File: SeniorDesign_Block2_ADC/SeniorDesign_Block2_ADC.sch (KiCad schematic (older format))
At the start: 2 parts

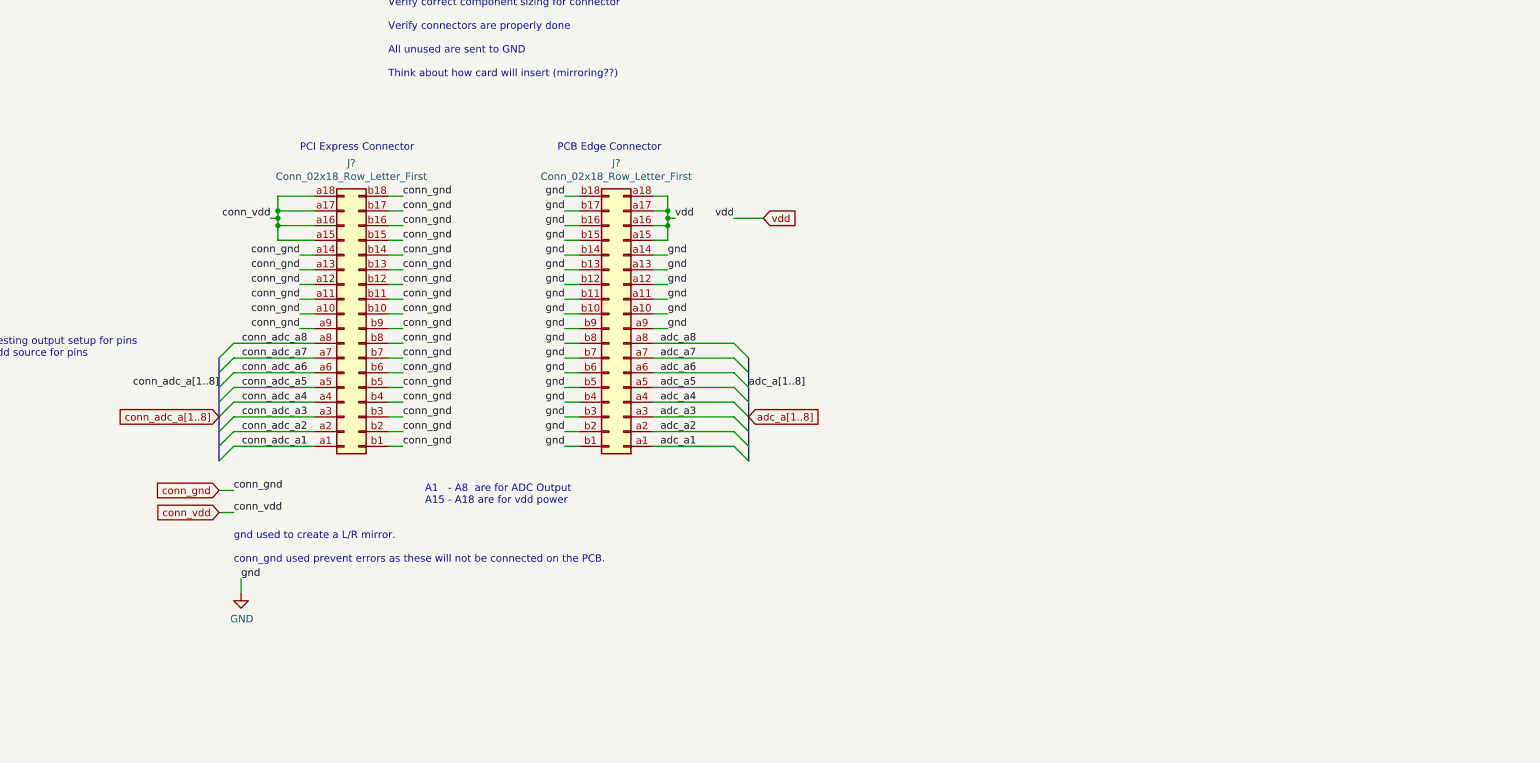
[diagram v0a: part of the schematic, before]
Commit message: Added ADC, oscillator, and misc parts associated to the two
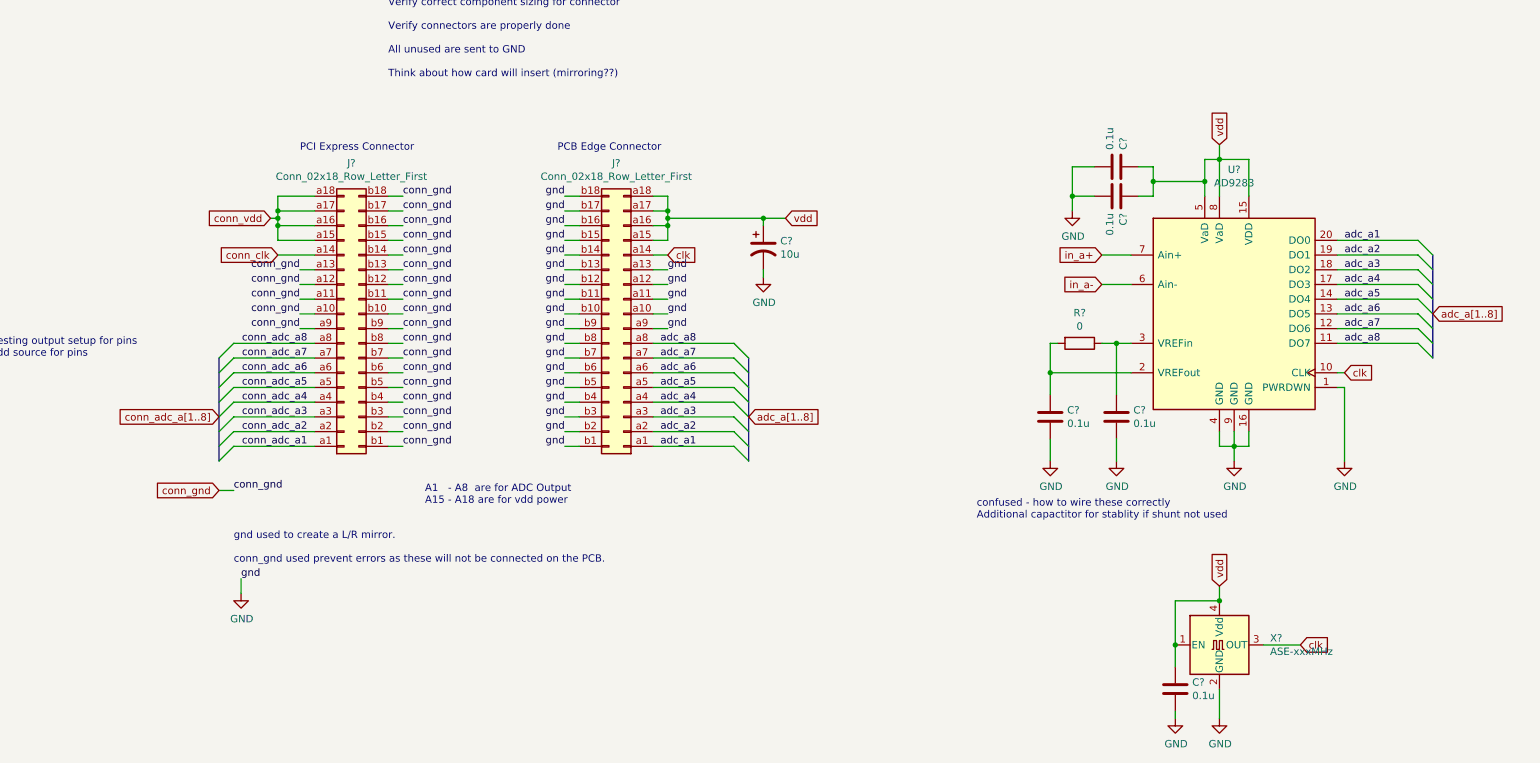
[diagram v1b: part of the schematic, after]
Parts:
- added C? (x5): 0.1u, Capacitor_SMD:C_0603_1608Metric, symbol Device:C
- added C?: 10u, Capacitor_SMD:CP_Elec_4x3.9, symbol Device:CP1
- added R?: 0, Resistor_SMD:R_0612_1632Metric_Pad1.18x3.40mm_HandSolder, symbol Device:R
- added U?: AD9283, symbol Analog_ADC:AD9283
- added X?: ASE-xxxMHz, SeniorDesign_Block2_ADC:DSC6001JI1A_Oscillator, symbol Oscillator:ASE-xxxMHz
- J?: part_url (none) -> NA
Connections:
- net GND: now also C?.2, C?.2, C?.2, C?.2, C?.2, C?.2, U?.1 (PWRDWN), U?.16 (GND), U?.4 (GND), U?.9 (GND), X?.2 (GND); no longer J?.a14 (Pin_a14)
- net adc_a1: now also U?.20 (DO0)
- net adc_a2: now also U?.19 (DO1)
- net adc_a3: now also U?.18 (DO2)
- net adc_a4: now also U?.17 (DO3)
- net adc_a5: now also U?.14 (DO4)
- net adc_a6: now also U?.13 (DO5)
- net adc_a7: now also U?.12 (DO6)
- net adc_a8: now also U?.11 (DO7)
- net conn_gnd: no longer J?.a14 (Pin_a14)
- net vdd: now also C?.1, C?.1, C?.1, C?.1, U?.15 (VDD), U?.5 (VaD), U?.8 (VaD), X?.1 (EN), X?.4 (Vdd)
- new net: C?.1, R?.2, U?.2 (VREFout)
- new net: C?.1, R?.1, U?.3 (VREFin)
- new net clk: J?.a14 (Pin_a14), U?.10 (CLK), X?.3 (OUT)
- new net conn_clk: J?.a14 (Pin_a14)
- new net in_a+: U?.7 (Ain+)
- new net in_a-: U?.6 (Ain-)
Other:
- note added: "confused - how to wire these correctly\nAdditional capactitor for stablity if shunt not used\n"

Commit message: Base shcematic complete.  Converting to PCB with misc connection errors.
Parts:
- added C3, C4: 56pF +/-5%, Capacitor_SMD:C_0603_1608Metric, symbol Device:C
- added D1: LED, LED_SMD:LED_1206_3216Metric, symbol Device:LED
- added R1, R2: 49.9 +/-1%, Resistor_SMD:R_0603_1608Metric_Pad0.98x0.95mm_HandSolder, symbol Device:R
- added R4: 0, Resistor_SMD:R_0612_1632Metric_Pad1.18x3.40mm_HandSolder, symbol Device:R
- added R5: 470, Resistor_SMD:R_0603_1608Metric_Pad0.98x0.95mm_HandSolder, symbol Device:R
- C1, C2, C5, C6, C8: renamed from C?; part_url (none) -> https://www.digikey.com/en/products/detail/samsung-electro-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
- R3: renamed from R?; part_url (none) -> NA
- U1: renamed from U?; footprint (none) -> Package_SO:SSOP-20_5.3x7.2mm_P0.65mm
- gave numbers to parts that had none: 4
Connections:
- net GND: now also C3.2, C4.2, D1.1 (K), R4.2; no longer U1.1 (PWRDWN)
- net in_a+: now also R1.2; no longer U1.7 (Ain+)
- net in_a-: now also R2.2; no longer U1.6 (Ain-)
- net vdd: now also R5.1
- new net: R4.1, U1.1 (PWRDWN)
- new net: C4.1, R2.1, U1.6 (Ain-)
- new net: C3.1, R1.1, U1.7 (Ain+)
- new net: D1.2 (A), R5.2
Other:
- note added: "LOW PASS FILTER\n50Mhz so that the project can use fun frequencies while cutting out noise.\n\nThe ADC has an input resistance of 10kohms and 2 pF of capactitance. \nFor simplicity, these are treated as both going to ground. \n\n---[ 50 ohm]---+----+-------+\n | | |\n [61pF] [2pF] [ 10k ohm]\n GROUND\n-3dB at 50Mhz."
- note added: "Power on indication"
- note removed: "A1 - A8 are for ADC Output\nA15 - A18 are for vdd power\n"
- note removed: "confused - how to wire these correctly\nAdditional capactitor for stablity if shunt not used\n"
- moved on the sheet: C1, C2, C5, C6, C8, R3, U1, X1
